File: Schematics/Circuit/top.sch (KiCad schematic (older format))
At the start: 12 parts

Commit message: Edit schematic and model
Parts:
- added R?: 150, symbol R
- C? (x6): symbol C -> C-RESCUE-top
- D?: symbol LED -> LED-RESCUE-top
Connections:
- wire segments 57 -> 58
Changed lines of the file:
@@
 EESchema Schematic File Version 2
+LIBS:top-rescue
 LIBS:power
 LIBS:device
+LIBS:switches
+LIBS:relays
+LIBS:motors
 LIBS:transistors
 LIBS:conn
@@
 LIBS:memory
 LIBS:xilinx
-LIBS:special
 LIBS:microcontrollers
 LIBS:dsp
@@
 LIBS:valves
 LIBS:top-cache
-LIBS:cansat-cache
-EELAYER 27 0
+EELAYER 25 0
 EELAYER END
 $Descr A4 11693 8268
@@
 $EndComp
 $Comp
-L C C?
+L C-RESCUE-top C?
 U 1 1 5A4CC89B
 P 8750 2400
@@
 $EndComp
 $Comp
-L C C?
+L C-RESCUE-top C?
 U 1 1 5A4CC89C
 P 9050 2400
@@
 $EndComp
 $Comp
-L GND #PWR?
+L GND-RESCUE-top #PWR?
 U 1 1 5A4CC89D
 P 9050 2700
@@
 RST
 $Comp
-L GND #PWR?
+L GND-RESCUE-top #PWR?
 U 1 1 5A4CC89E
 P 9650 1150
@@
 $EndComp
 $Comp
-L +3.3V #PWR?
+L +3.3V-RESCUE-top #PWR?
 U 1 1 5A4CC8A1
 P 9300 2100
@@
 $EndComp
 $Comp
-L GND #PWR?
+L GND-RESCUE-top #PWR?
 U 1 1 5A4CC8A2
 P 8400 6200
@@
 $EndComp
 $Comp
-L C C?
+L C-RESCUE-top C?
 U 1 1 5A4CC8A4
 P 10550 5800
@@
 SCL
 $Comp
-L GND #PWR?
+L GND-RESCUE-top #PWR?
 U 1 1 5A4CC8A5
 P 10800 6100
@@
 $EndComp
 $Comp
-L +3.3V #PWR?
+L +3.3V-RESCUE-top #PWR?
 U 1 1 5A4CC8A6
 P 10750 6000
@@
 $EndComp
 $Comp
-L LED D?
+L LED-RESCUE-top D?
 U 1 1 5A4CC8A7
 P 9800 3250
@@
 $EndComp
 $Comp
-L GND #PWR?
+L GND-RESCUE-top #PWR?
 U 1 1 5A4CC8A8
 P 10450 3250
@@
 	10000 3250 10450 3250
 Wire Wire Line
-	9600 3250 9050 3250
-Wire Wire Line
 	8800 6100 8600 6100
 Wire Wire Line
@@
 SCL
 $Comp
-L +3.3V #PWR?
+L +3.3V-RESCUE-top #PWR?
 U 1 1 5A4CC8D7
 P 10550 4500
@@
 $EndComp
 $Comp
-L C C?
+L C-RESCUE-top C?
 U 1 1 5A4CC8D8
 P 10700 4800
@@
 $EndComp
 $Comp
-L C C?
+L C-RESCUE-top C?
 U 1 1 5A4CC8D9
 P 8650 4500
@@
 $EndComp
 $Comp
-L C C?
+L C-RESCUE-top C?
 U 1 1 5A4CC8DA
 P 8750 5100
@@
 $EndComp
 $Comp
-L GND #PWR?
+L GND-RESCUE-top #PWR?
 U 1 1 5A4CC8DB
 P 10900 4600
@@
 $EndComp
 $Comp
-L GND #PWR?
+L GND-RESCUE-top #PWR?
 U 1 1 5A4CC94F
 P 7700 4550
@@
 $EndComp
 $Comp
-L +3.3V #PWR?
+L +3.3V-RESCUE-top #PWR?
 U 1 1 5A4CC96D
 P 7700 4450
@@
 Wire Wire Line
 	7350 4550 7700 4550
+$Comp
+L R R?
+U 1 1 5A51DC75
+P 9200 3250
+F 0 "R?" V 9280 3250 50  0000 C CNN
+F 1 "150" V 9200 3250 50  0000 C CNN
+F 2 "" V 9130 3250 50  0001 C CNN
+F 3 "" H 9200 3250 50  0001 C CNN
+	1    9200 3250
+	0    1    1    0
+$EndComp
+Wire Wire Line
+	9350 3250 9600 3250
+Wire Wire Line
+	9050 3250 8600 3250
+Text Label 8600 3250 0    60   ~ 0
+LED
 $EndSCHEMATC

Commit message: Edit schematic and footprints
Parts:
- C1, C4, C5, C6: renamed from C?; footprint ~ -> Capacitors_SMD:C_0805
- C2, C3: renamed from C?; footprint ~ -> Capacitors_SMD:C_0402
- D1: renamed from D?; footprint ~ -> Diodes_SMD:D_0603
- gave numbers to parts that had none: 6
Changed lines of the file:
@@
 $EndDescr
 $Comp
-L HIH9131 IC?
+L HIH9131 IC3
 U 1 1 5A4CC89A
 P 9900 2450
-F 0 "IC?" H 9650 2700 60  0000 C CNN
+F 0 "IC3" H 9650 2700 60  0000 C CNN
 F 1 "HIH9131" H 10000 2200 60  0000 C CNN
-F 2 "" H 9900 2450 60  0000 C CNN
+F 2 "" H 9900 2450 60  0001 C CNN
 F 3 "" H 9900 2450 60  0000 C CNN
 	1    9900 2450
@@
 $EndComp
 $Comp
-L C-RESCUE-top C?
+L C-RESCUE-top C2
 U 1 1 5A4CC89B
 P 8750 2400
-F 0 "C?" H 8750 2500 40  0000 L CNN
+F 0 "C2" H 8750 2500 40  0000 L CNN
 F 1 "0.22 uF" H 8756 2315 40  0000 L CNN
-F 2 "~" H 8788 2250 30  0000 C CNN
+F 2 "Capacitors_SMD:C_0402" H 8788 2250 30  0000 C CNN
 F 3 "~" H 8750 2400 60  0000 C CNN
 	1    8750 2400
@@
 $EndComp
 $Comp
-L C-RESCUE-top C?
+L C-RESCUE-top C4
 U 1 1 5A4CC89C
 P 9050 2400
-F 0 "C?" H 9050 2500 40  0000 L CNN
+F 0 "C4" H 9050 2500 40  0000 L CNN
 F 1 "100 nF" H 9056 2315 40  0000 L CNN
-F 2 "~" H 9088 2250 30  0000 C CNN
+F 2 "Capacitors_SMD:C_0805" H 9088 2250 30  0000 C CNN
 F 3 "~" H 9050 2400 60  0000 C CNN
 	1    9050 2400
@@
 $EndComp
 $Comp
-L GND-RESCUE-top #PWR?
+L GND-RESCUE-top #PWR01
 U 1 1 5A4CC89D
 P 9050 2700
-F 0 "#PWR?" H 9050 2700 30  0001 C CNN
+F 0 "#PWR01" H 9050 2700 30  0001 C CNN
 F 1 "GND" H 9050 2630 30  0001 C CNN
 F 2 "" H 9050 2700 60  0000 C CNN
@@
 RST
 $Comp
-L GND-RESCUE-top #PWR?
+L GND-RESCUE-top #PWR02
 U 1 1 5A4CC89E
 P 9650 1150
-F 0 "#PWR?" H 9650 1150 30  0001 C CNN
+F 0 "#PWR02" H 9650 1150 30  0001 C CNN
 F 1 "GND" H 9650 1080 30  0001 C CNN
 F 2 "" H 9650 1150 60  0000 C CNN
@@
 $EndComp
 $Comp
-L CONN_6 P?
+L CONN_6 P2
 U 1 1 5A4CC89F
 P 10200 900
-F 0 "P?" V 10150 900 60  0000 C CNN
+F 0 "P2" V 10150 900 60  0000 C CNN
 F 1 "USB CONN" V 10250 900 60  0000 C CNN
-F 2 "" H 10200 900 60  0000 C CNN
+F 2 "" H 10200 900 60  0001 C CNN
 F 3 "" H 10200 900 60  0000 C CNN
 	1    10200 900
@@
 RX
 $Comp
-L +5V #PWR?
+L +5V #PWR03
 U 1 1 5A4CC8A0
 P 9650 950
-F 0 "#PWR?" H 9650 1040 20  0001 C CNN
+F 0 "#PWR03" H 9650 1040 20  0001 C CNN
 F 1 "+5V" H 9650 1040 30  0000 C CNN
 F 2 "" H 9650 950 60  0000 C CNN
@@
 $EndComp
 $Comp
-L +3.3V-RESCUE-top #PWR?
+L +3.3V-RESCUE-top #PWR04
 U 1 1 5A4CC8A1
 P 9300 2100
-F 0 "#PWR?" H 9300 2060 30  0001 C CNN
+F 0 "#PWR04" H 9300 2060 30  0001 C CNN
 F 1 "+3.3V" H 9300 2210 30  0000 C CNN
 F 2 "" H 9300 2100 60  0000 C CNN
@@
 $EndComp
 $Comp
-L GND-RESCUE-top #PWR?
+L GND-RESCUE-top #PWR05
 U 1 1 5A4CC8A2
 P 8400 6200
-F 0 "#PWR?" H 8400 6200 30  0001 C CNN
+F 0 "#PWR05" H 8400 6200 30  0001 C CNN
 F 1 "GND" H 8400 6130 30  0001 C CNN
 F 2 "" H 8400 6200 60  0000 C CNN
@@
 $EndComp
 $Comp
-L LPS22HB IC?
+L LPS22HB IC1
 U 1 1 5A4CC8A3
 P 9600 6200
-F 0 "IC?" H 9200 6550 60  0000 C CNN
+F 0 "IC1" H 9200 6550 60  0000 C CNN
 F 1 "LPS22HB" H 9900 5850 60  0000 C CNN
-F 2 "" H 9600 6200 60  0000 C CNN
+F 2 "" H 9600 6200 60  0001 C CNN
 F 3 "" H 9600 6200 60  0000 C CNN
 	1    9600 6200
@@
 $EndComp
 $Comp
-L C-RESCUE-top C?
+L C-RESCUE-top C5
 U 1 1 5A4CC8A4
 P 10550 5800
-F 0 "C?" H 10550 5900 40  0000 L CNN
+F 0 "C5" H 10550 5900 40  0000 L CNN
 F 1 "100 nF" H 10556 5715 40  0000 L CNN
-F 2 "~" H 10588 5650 30  0000 C CNN
+F 2 "Capacitors_SMD:C_0805" H 10588 5650 30  0000 C CNN
 F 3 "~" H 10550 5800 60  0000 C CNN
 	1    10550 5800
@@
 SCL
 $Comp
-L GND-RESCUE-top #PWR?
+L GND-RESCUE-top #PWR06
 U 1 1 5A4CC8A5
 P 10800 6100
-F 0 "#PWR?" H 10800 6100 30  0001 C CNN
+F 0 "#PWR06" H 10800 6100 30  0001 C CNN
 F 1 "GND" H 10800 6030 30  0001 C CNN
 F 2 "" H 10800 6100 60  0000 C CNN
@@
 $EndComp
 $Comp
-L +3.3V-RESCUE-top #PWR?
+L +3.3V-RESCUE-top #PWR07
 U 1 1 5A4CC8A6
 P 10750 6000
-F 0 "#PWR?" H 10750 6090 20  0001 C CNN
+F 0 "#PWR07" H 10750 6090 20  0001 C CNN
 F 1 "+3.3V" H 10750 6090 30  0000 C CNN
 F 2 "" H 10750 6000 60  0000 C CNN
@@
 $EndComp
 $Comp
-L LED-RESCUE-top D?
+L LED-RESCUE-top D1
 U 1 1 5A4CC8A7
 P 9800 3250
-F 0 "D?" H 9800 3350 50  0000 C CNN
+F 0 "D1" H 9800 3350 50  0000 C CNN
 F 1 "LED" H 9800 3150 50  0000 C CNN
-F 2 "~" H 9800 3250 60  0000 C CNN
+F 2 "Diodes_SMD:D_0603" H 9800 3250 60  0000 C CNN
 F 3 "~" H 9800 3250 60  0000 C CNN
 	1    9800 3250
@@
 $EndComp
 $Comp
-L GND-RESCUE-top #PWR?
+L GND-RESCUE-top #PWR08
 U 1 1 5A4CC8A8
 P 10450 3250
-F 0 "#PWR?" H 10450 3250 30  0001 C CNN
+F 0 "#PWR08" H 10450 3250 30  0001 C CNN
 F 1 "GND" H 10450 3180 30  0001 C CNN
 F 2 "" H 10450 3250 60  0000 C CNN
@@
 	8750 2200 8750 2100
 $Comp
-L HMC5883L IC?
+L HMC5883L IC2
 U 1 1 5A4CC8D6
 P 9650 4550
-F 0 "IC?" H 9400 5050 60  0000 C CNN
+F 0 "IC2" H 9400 5050 60  0000 C CNN
 F 1 "HMC5883L" H 9700 4050 60  0000 C CNN
-F 2 "" H 9650 4550 60  0000 C CNN
+F 2 "" H 9650 4550 60  0001 C CNN
 F 3 "" H 9650 4550 60  0000 C CNN
 	1    9650 4550
@@
 SCL
 $Comp
-L +3.3V-RESCUE-top #PWR?
+L +3.3V-RESCUE-top #PWR09
 U 1 1 5A4CC8D7
 P 10550 4500
-F 0 "#PWR?" H 10550 4460 30  0001 C CNN
+F 0 "#PWR09" H 10550 4460 30  0001 C CNN
 F 1 "+3.3V" H 10550 4610 30  0000 C CNN
 F 2 "" H 10550 4500 60  0000 C CNN
@@
 $EndComp
 $Comp
-L C-RESCUE-top C?
+L C-RESCUE-top C6
 U 1 1 5A4CC8D8
 P 10700 4800
-F 0 "C?" H 10700 4900 40  0000 L CNN
+F 0 "C6" H 10700 4900 40  0000 L CNN
 F 1 "4.7 uF" H 10706 4715 40  0000 L CNN
-F 2 "~" H 10738 4650 30  0000 C CNN
+F 2 "Capacitors_SMD:C_0805" H 10738 4650 30  0000 C CNN
 F 3 "~" H 10700 4800 60  0000 C CNN
 	1    10700 4800
@@
 $EndComp
 $Comp
-L C-RESCUE-top C?
+L C-RESCUE-top C1
 U 1 1 5A4CC8D9
 P 8650 4500
-F 0 "C?" H 8650 4600 40  0000 L CNN
+F 0 "C1" H 8650 4600 40  0000 L CNN
 F 1 "100 nF" H 8656 4415 40  0000 L CNN
-F 2 "~" H 8688 4350 30  0000 C CNN
+F 2 "Capacitors_SMD:C_0805" H 8688 4350 30  0000 C CNN
 F 3 "~" H 8650 4500 60  0000 C CNN
 	1    8650 4500
@@
 $EndComp
 $Comp
-L C-RESCUE-top C?
+L C-RESCUE-top C3
 U 1 1 5A4CC8DA
 P 8750 5100
-F 0 "C?" H 8750 5200 40  0000 L CNN
+F 0 "C3" H 8750 5200 40  0000 L CNN
 F 1 "0.22 uF" H 8756 5015 40  0000 L CNN
-F 2 "~" H 8788 4950 30  0000 C CNN
+F 2 "Capacitors_SMD:C_0402" H 8788 4950 30  0000 C CNN
 F 3 "~" H 8750 5100 60  0000 C CNN
 	1    8750 5100
@@
 $EndComp
 $Comp
-L GND-RESCUE-top #PWR?
+L GND-RESCUE-top #PWR010
 U 1 1 5A4CC8DB
 P 10900 4600
-F 0 "#PWR?" H 10900 4600 30  0001 C CNN
+F 0 "#PWR010" H 10900 4600 30  0001 C CNN
 F 1 "GND" H 10900 4530 30  0001 C CNN
 F 2 "" H 10900 4600 60  0000 C CNN
@@
 	10550 5400 10550 4900
 $Comp
-L CONN_9 P?
+L CONN_9 P1
 U 1 1 5A4CC903
 P 7000 4150
-F 0 "P?" V 6950 4150 60  0000 C CNN
+F 0 "P1" V 6950 4150 60  0000 C CNN
 F 1 "CONN_9" V 7050 4150 60  0000 C CNN
-F 2 "" H 7000 4150 60  0000 C CNN
+F 2 "" H 7000 4150 60  0001 C CNN
 F 3 "" H 7000 4150 60  0000 C CNN
 	1    7000 4150
@@
 $EndComp
 $Comp
-L GND-RESCUE-top #PWR?
+L GND-RESCUE-top #PWR011
 U 1 1 5A4CC94F
 P 7700 4550
-F 0 "#PWR?" H 7700 4550 30  0001 C CNN
+F 0 "#PWR011" H 7700 4550 30  0001 C CNN
 F 1 "GND" H 7700 4480 30  0001 C CNN
 F 2 "" H 7700 4550 60  0000 C CNN
@@
 $EndComp
 $Comp
-L +3.3V-RESCUE-top #PWR?
+L +3.3V-RESCUE-top #PWR012
 U 1 1 5A4CC96D
 P 7700 4450
-F 0 "#PWR?" H 7700 4410 30  0001 C CNN
+F 0 "#PWR012" H 7700 4410 30  0001 C CNN
 F 1 "+3.3V" H 7700 4560 30  0000 C CNN
 F 2 "" H 7700 4450 60  0000 C CNN
@@
 $EndComp
 $Comp
-L +5V #PWR?
+L +5V #PWR013
 U 1 1 5A4CC98B
 P 7650 4350
-F 0 "#PWR?" H 7650 4440 20  0001 C CNN
+F 0 "#PWR013" H 7650 4440 20  0001 C CNN
 F 1 "+5V" H 7650 4440 30  0000 C CNN
 F 2 "" H 7650 4350 60  0000 C CNN
@@
 	7350 4550 7700 4550
 $Comp
-L R R?
+L R R1
 U 1 1 5A51DC75
 P 9200 3250
-F 0 "R?" V 9280 3250 50  0000 C CNN
+F 0 "R1" V 9280 3250 50  0000 C CNN
 F 1 "150" V 9200 3250 50  0000 C CNN
 F 2 "" V 9130 3250 50  0001 C CNN

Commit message: Edit finish circuits and some model work
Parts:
- removed IC2: HMC5883L, symbol HMC5883L
- removed P1: CONN_9, symbol CONN_9
- removed P2: USB CONN, symbol CONN_6
- added C7: 100 nF, Capacitors_SMD:C_0805, symbol C-RESCUE-top
- added J1: Conn_01x05, Pin_Headers:Pin_Header_Straight_1x05_Pitch1.27mm_SMD_Pin1Left, symbol Conn_01x05
- added U1: LSM303AGRTR, CanSat:LSM303AGRTR, symbol LSM303AGRTR
- C6: value 4.7 uF -> 10 uF
- IC1: footprint (none) -> LPS22HB:LGA10R50P2X3_200X200X80
- IC3: footprint (none) -> SOIC127P600X175-8N:SOIC127P600X175-8N
- R1: footprint (none) -> Resistors_SMD:R_0805
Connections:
- net labels removed: +5V, RST, RX, TX
- wire segments 58 -> 46
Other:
- moved on the sheet: C1, C3, C6

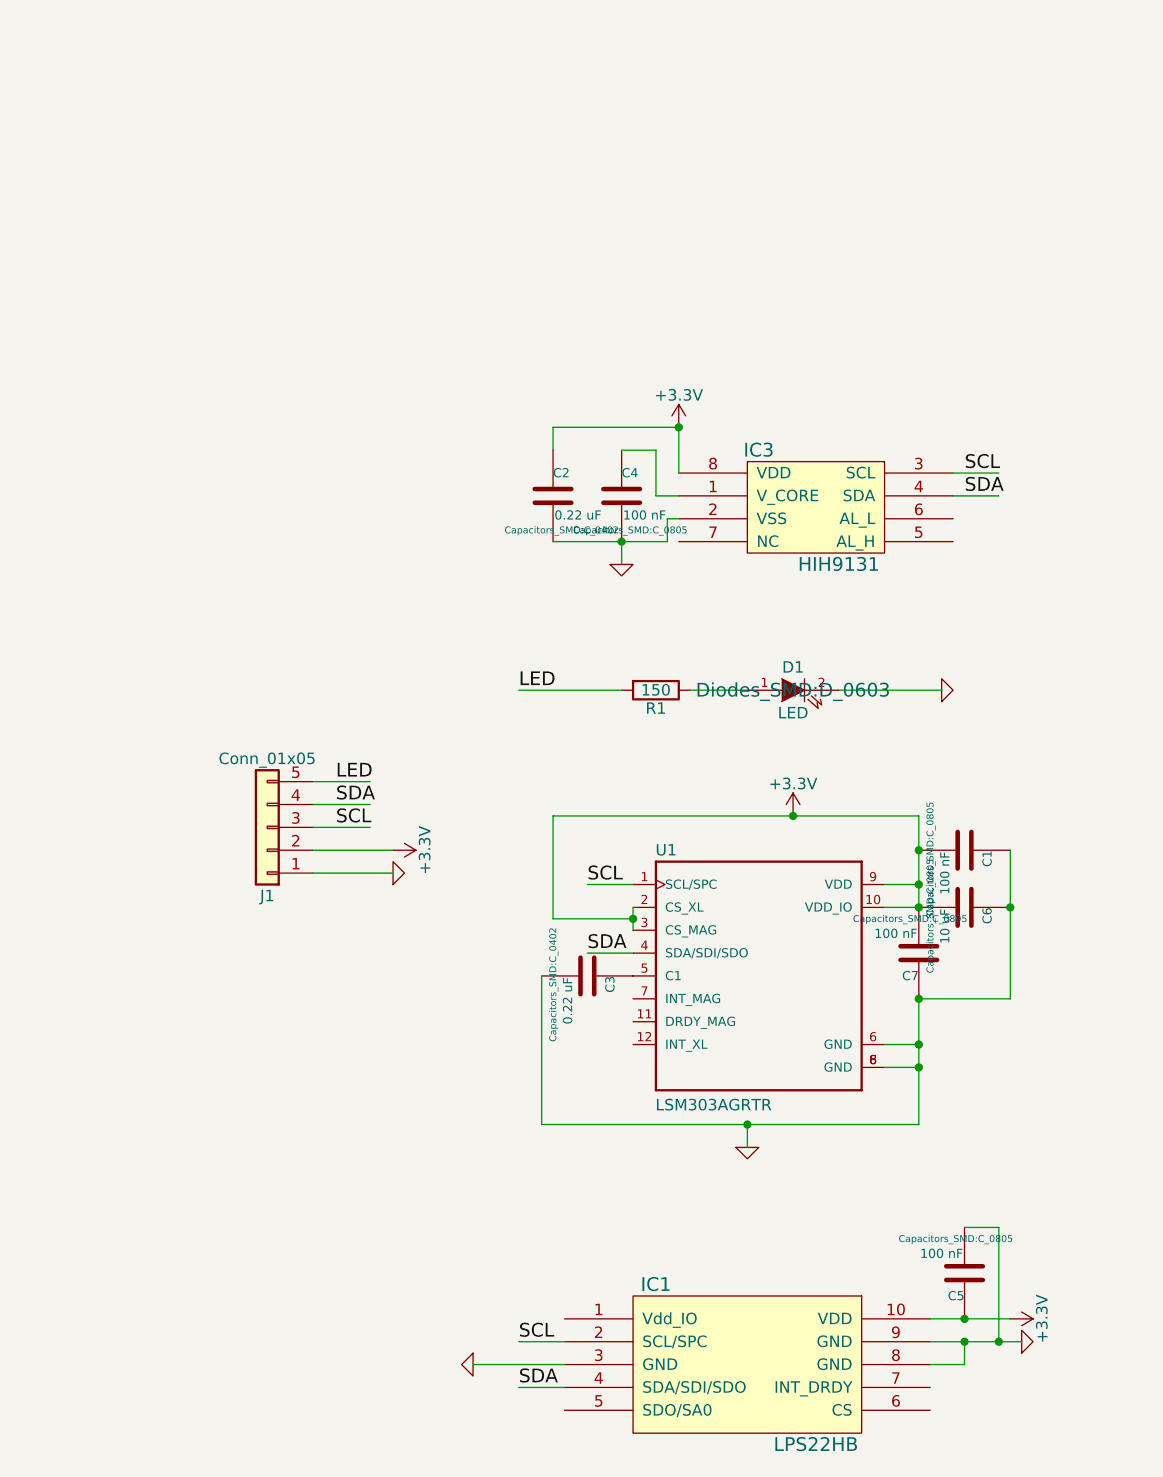
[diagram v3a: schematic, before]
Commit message: Add UV and Gamma detection, fix main pcb
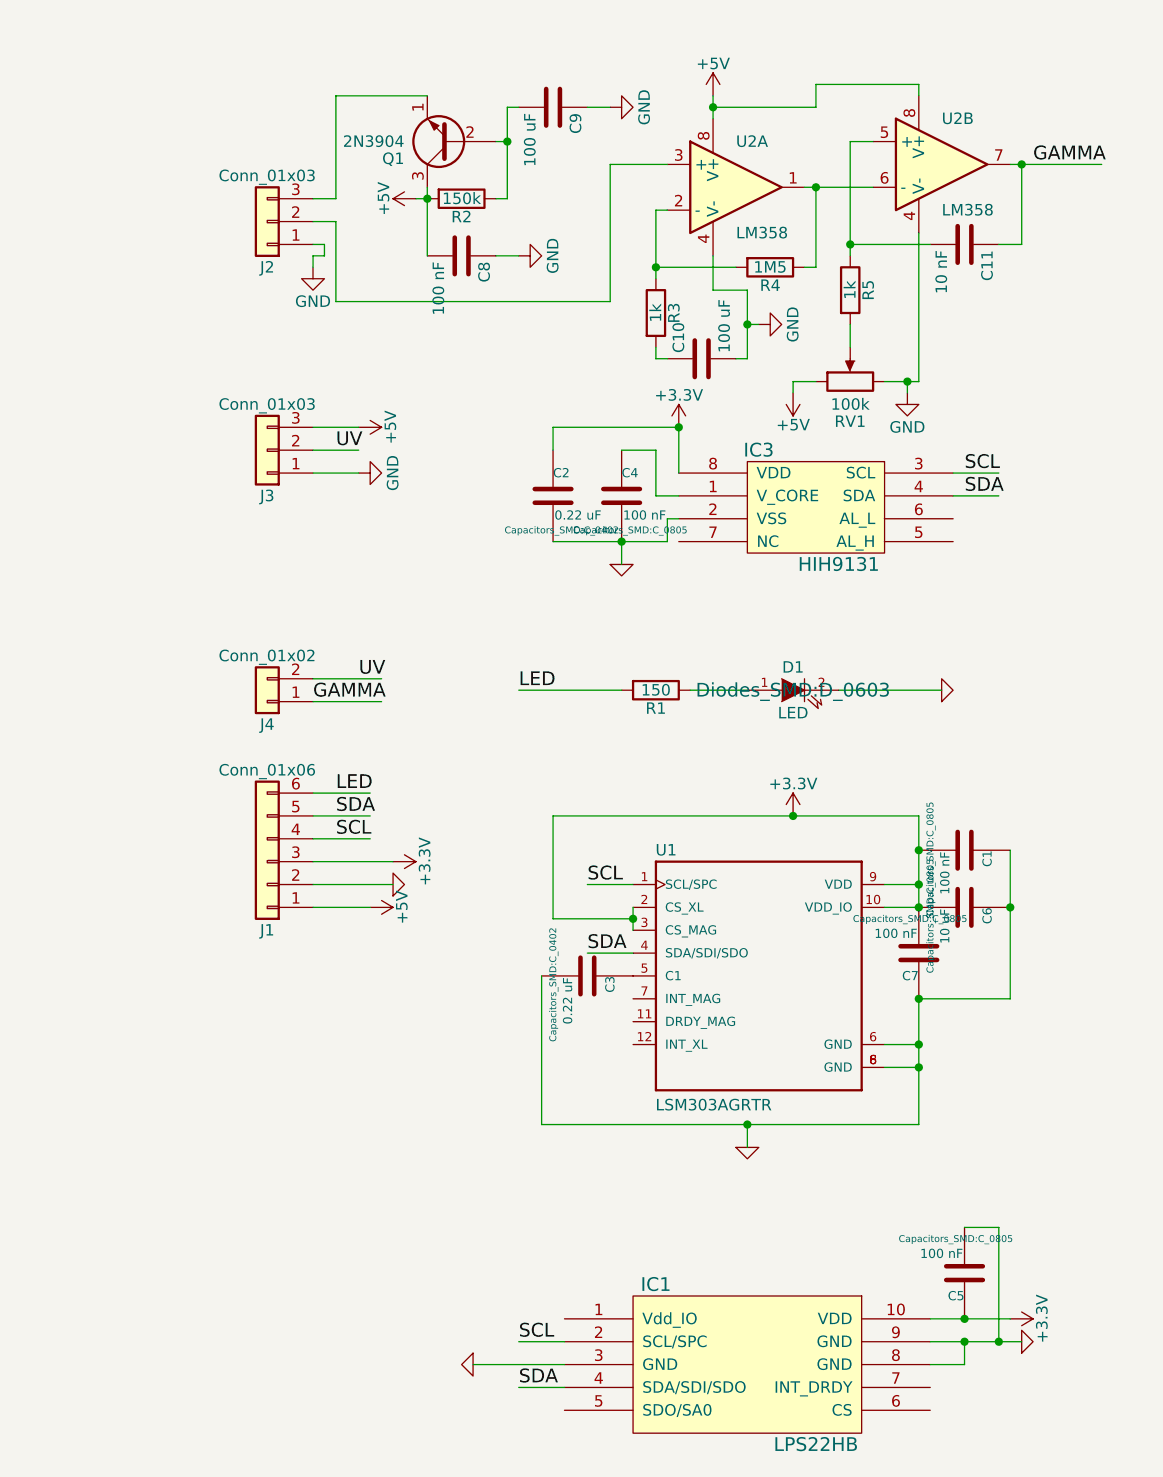
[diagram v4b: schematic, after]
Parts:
- removed J1: Conn_01x05, Pin_Headers:Pin_Header_Straight_1x05_Pitch1.27mm_SMD_Pin1Left, symbol Conn_01x05
- added C10, C9: 100 uF, Capacitors_Tantalum_SMD:CP_Tantalum_Case-A_EIA-3216-18_Reflow, symbol C
- added C11: 10 nF, Capacitors_SMD:C_0603, symbol C
- added C8: 100 nF, Capacitors_SMD:C_0805, symbol C
- added J1: Conn_01x06, Pin_Headers:Pin_Header_Straight_1x06_Pitch1.27mm_SMD_Pin1Left, symbol Conn_01x06
- added J2: Conn_01x03, CanSat:MOLEX_PicoBlade_3, symbol Conn_01x03
- added J3: Conn_01x03, Pin_Headers:Pin_Header_Straight_1x03_Pitch2.54mm, symbol Conn_01x03
- added J4: Conn_01x02, CanSat:MOLEX_PicoBlade_2, symbol Conn_01x02
- added Q1: 2N3904, TO_SOT_Packages_THT:TO-92_Molded_Narrow, symbol 2N3904
- added R2: 150k, Resistors_SMD:R_0603, symbol R
- added R3, R5: 1k, Resistors_SMD:R_0603, symbol R
- added R4: 1M5, Resistors_SMD:R_0603, symbol R
- added RV1: 100k, Pin_Headers:Pin_Header_Straight_1x03_Pitch2.54mm, symbol POT
- added U2: LM358, SOIC127P600X175-8N:SOIC127P600X175-8N, symbol LM358
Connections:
- net labels added: +5V, GAMMA, UV
- wire segments 46 -> 102
